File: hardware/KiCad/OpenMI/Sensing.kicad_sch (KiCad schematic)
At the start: 42 parts, among them U2 INA381A2IDGS, U5 MCP6004-SL, U7 MCP6001T-OT

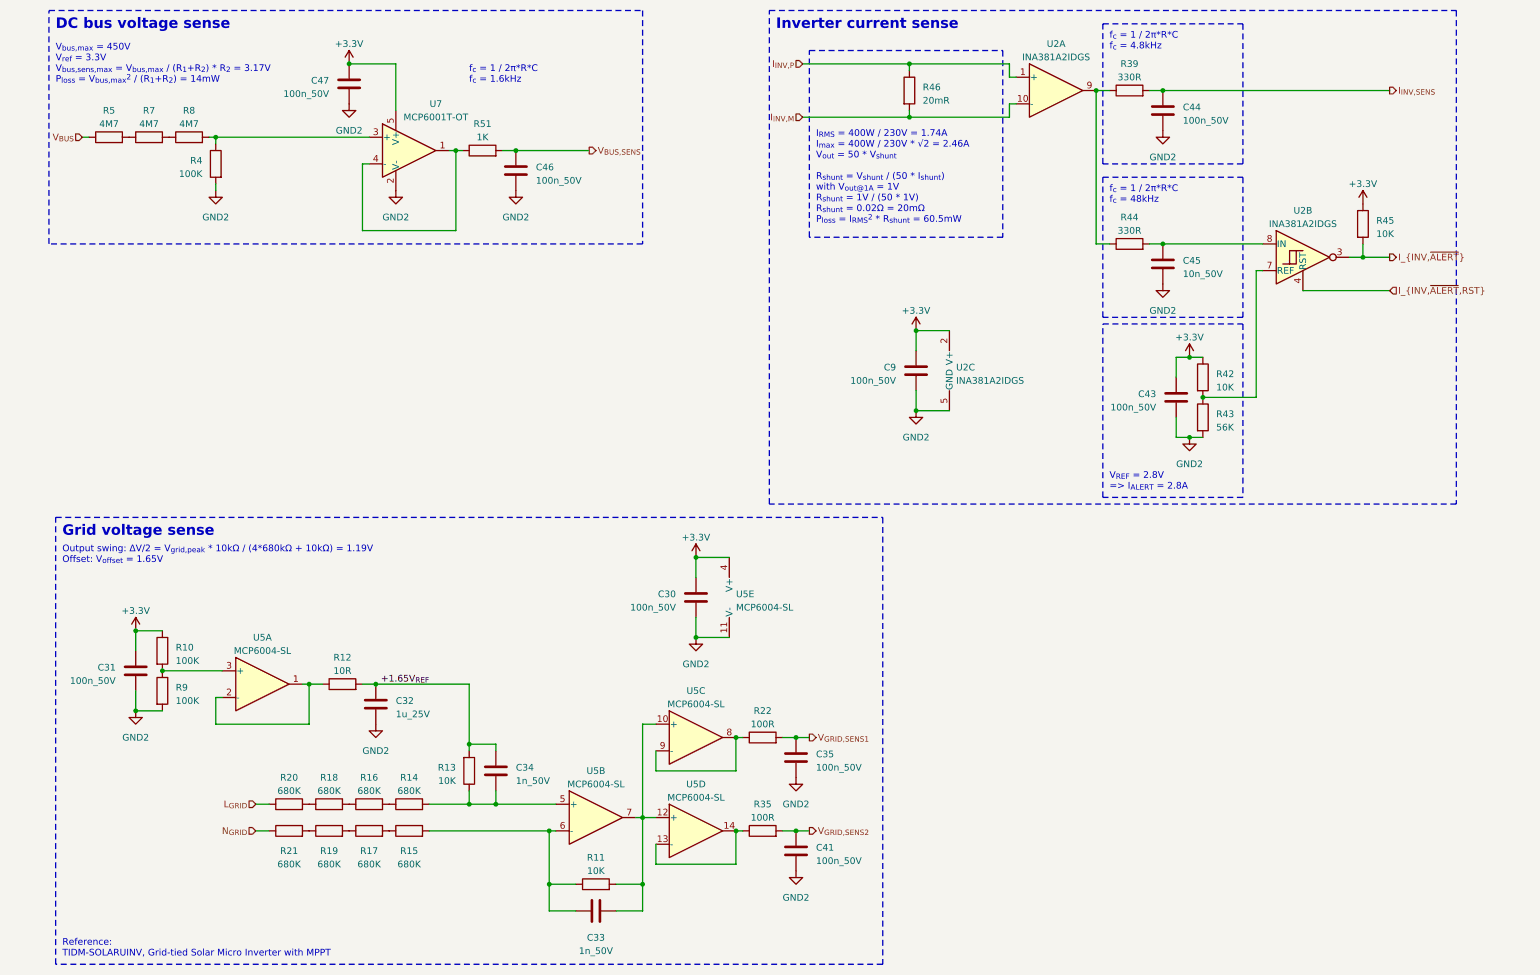
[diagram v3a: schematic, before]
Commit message: feat: Adds grid current sensing using a hall effect sensor.
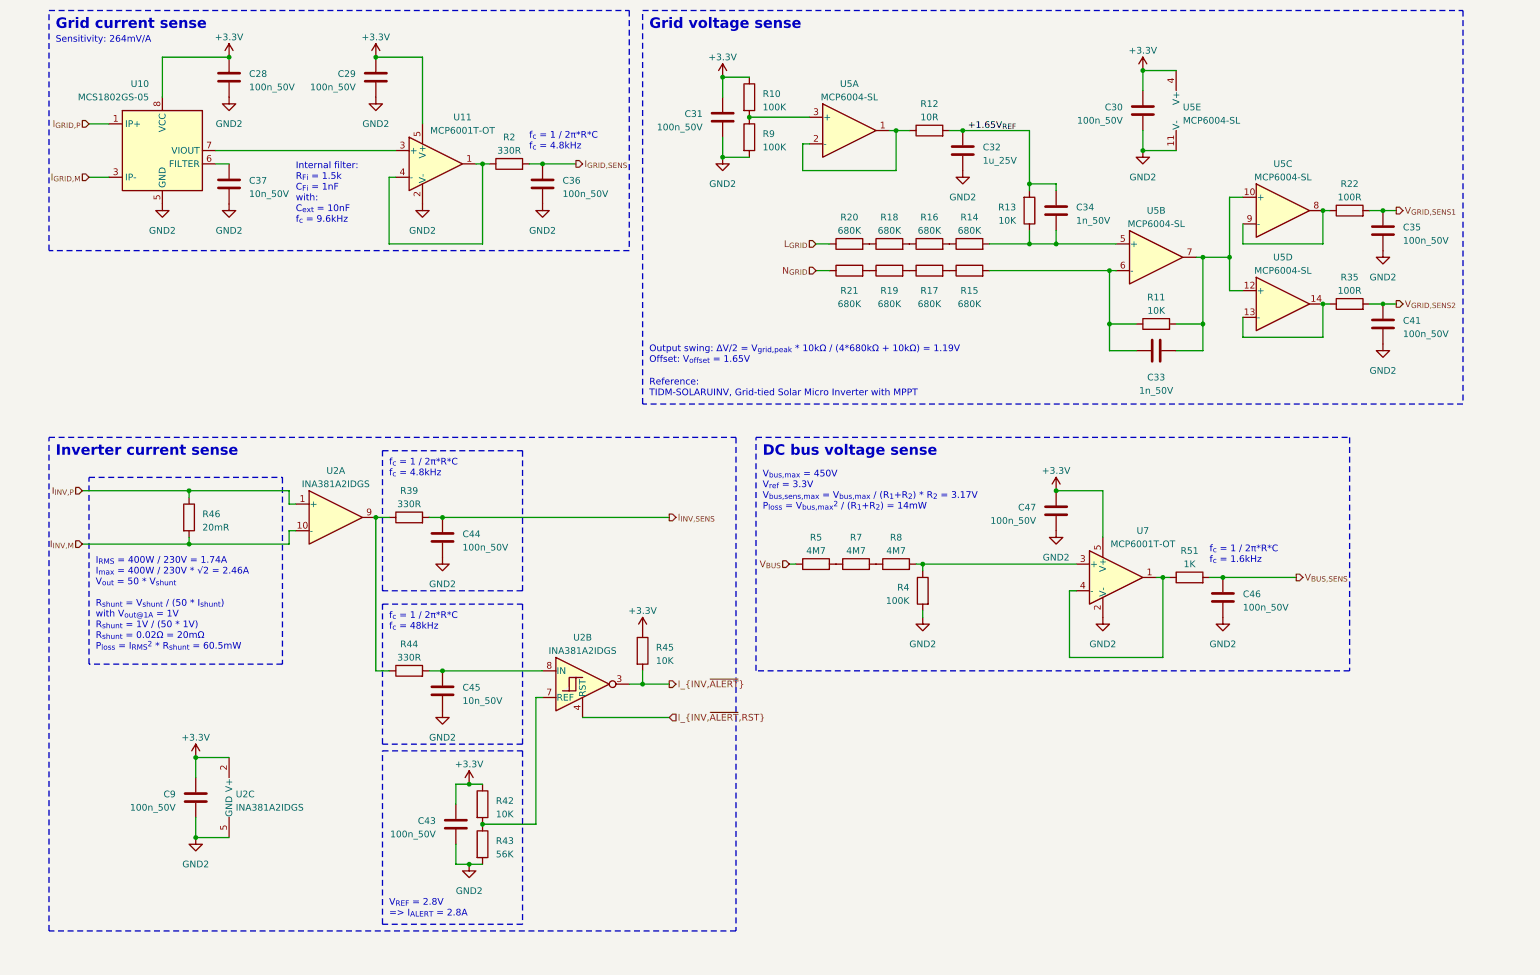
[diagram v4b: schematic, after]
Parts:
- added C28, C29, C36: 100n_50V, Capacitor_SMD:C_0603_1608Metric, symbol _C_0603:100n_50V
- added C37: 10n_50V, Capacitor_SMD:C_0603_1608Metric, symbol _C_0603:10n_50V
- added R2: 330R, Resistor_SMD:R_0603_1608Metric, symbol _R_0603:330R
- added U10: MCS1802GS-05, Package_SO:SOIC-8_3.9x4.9mm_P1.27mm, symbol _Amplifier_Current:MCS1802GS-05
- added U11: MCP6001T-OT, Package_TO_SOT_SMD:SOT-23-5, symbol _Amplifier_Operational:MCP6001T-OT
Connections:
- net +3.3V: now also C28.1, C29.1, U10.8 (VCC), U11.5 (V+)
- net GND2: now also C28.2, C29.2, C36.2, C37.2, U10.5 (GND), U11.2 (V-)
- new net: R2.1, U11.1, U11.4 (-)
- new net: U10.7 (VIOUT), U11.3 (+)
- new net: C37.1, U10.6 (FILTER)
- new net I_{GRID,M}: U10.3 (IP-), U10.4 (IP-)
- new net I_{GRID,P}: U10.1 (IP+), U10.2 (IP+)
- new net I_{GRID,SENS}: C36.1, R2.2
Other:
- note added: "Grid current sense"
- note added: "Internal filter: R_{Fi} = 1.5k C_{Fi} = 1nF with: C_{ext} = 10nF f_{c} = 9.6kHz"
- note added: "Sensitivity: 264mV/A"
- moved on the sheet: C30, C31, C32, C33, C34, C35, C41, C43, C44, C45, C46, C47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

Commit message: feat(hw): Adds grid current alert output to `Sensing`.
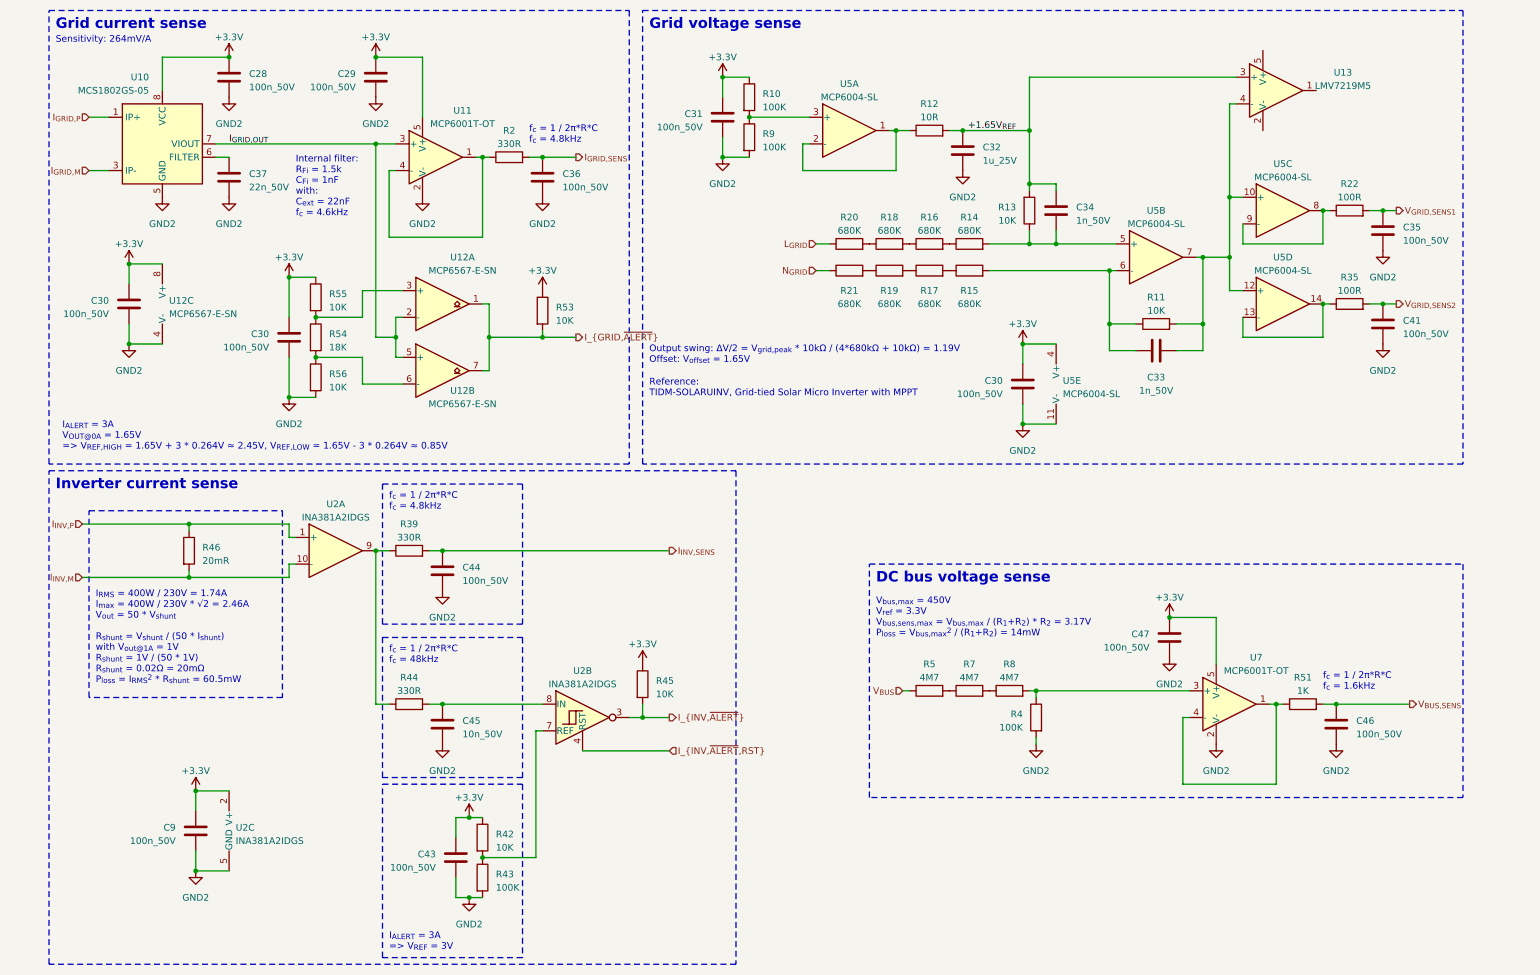
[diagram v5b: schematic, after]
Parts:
- removed C37: 10n_50V, Capacitor_SMD:C_0603_1608Metric, symbol _C_0603:10n_50V
- removed R43: 56K, Resistor_SMD:R_0603_1608Metric, symbol _R_0603:56K
- added C30 (x2): 100n_50V, Capacitor_SMD:C_0603_1608Metric, symbol _C_0603:100n_50V
- added C37: 22n_50V, Capacitor_SMD:C_0603_1608Metric, symbol _C_0603:22n_50V
- added R43: 100K, Resistor_SMD:R_0603_1608Metric, symbol _R_0603:100K
- added R53, R55, R56: 10K, Resistor_SMD:R_0603_1608Metric, symbol _R_0603:10K
- added R54: 18K, Resistor_SMD:R_0603_1608Metric, symbol _R_0603:18K
- added U12: MCP6567-E-SN, Package_SO:SOIC-8_3.9x4.9mm_P1.27mm, symbol _Comparator:MCP6567-E-SN
- added U13: LMV7219M5, Package_TO_SOT_SMD:SOT-23-5, symbol Comparator:LMV7219M5
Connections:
- net +1.65V_{REF}: now also U13.3 (+)
- net +3.3V: now also C30.1, C30.1, R53.1, R55.1, U12.8 (V+)
- net GND2: now also C30.2, C30.2, C37.2, R43.2, R56.2, U12.4 (V-)
- net at R42.2, U2.7 (REF): now also R43.1
- net I_{GRID,OUT}: now reaches U10.7 (VIOUT), U11.3 (+)
- net I_{GRID,OUT}: now also U12.2 (-), U12.5 (+)
- net at C33.2, R11.2, U5.10 (+)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: now also U13.4 (-)
- net at U10.6 (FILTER): now also C37.1
- new net: R54.1, R55.2, U12.3 (+)
- new net: R54.2, R56.1, U12.6 (-)
- new net I_{GRID,~{ALERT}}: R53.2, U12.1, U12.7
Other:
- note added: "I_{ALERT} = 3A => V_{REF} = 3V"
- note added: "I_{ALERT} = 3A V_{OUT@0A} = 1.65V => V_{REF,HIGH} = 1.65V + 3 * 0.264V ≈ 2.45V, V_{REF,LOW} = 1.65V - 3 * 0.264V ≈ 0.85V"
- note added: "Internal filter: R_{Fi} = 1.5k C_{Fi} = 1nF with: C_{ext} = 22nF f_{c} = 4.6kHz"
- note removed: "Internal filter: R_{Fi} = 1.5k C_{Fi} = 1nF with: C_{ext} = 10nF f_{c} = 9.6kHz"
- note removed: "V_{REF} = 2.8V => I_{ALERT} = 2.8A"
- moved on the sheet: C30, C36, C43, C44, C45, C46, C47, C9, R2, R39, R4, R42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

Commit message: feat(hw): Adds zero-crossing-detection (ZCD) to `Sensing`.
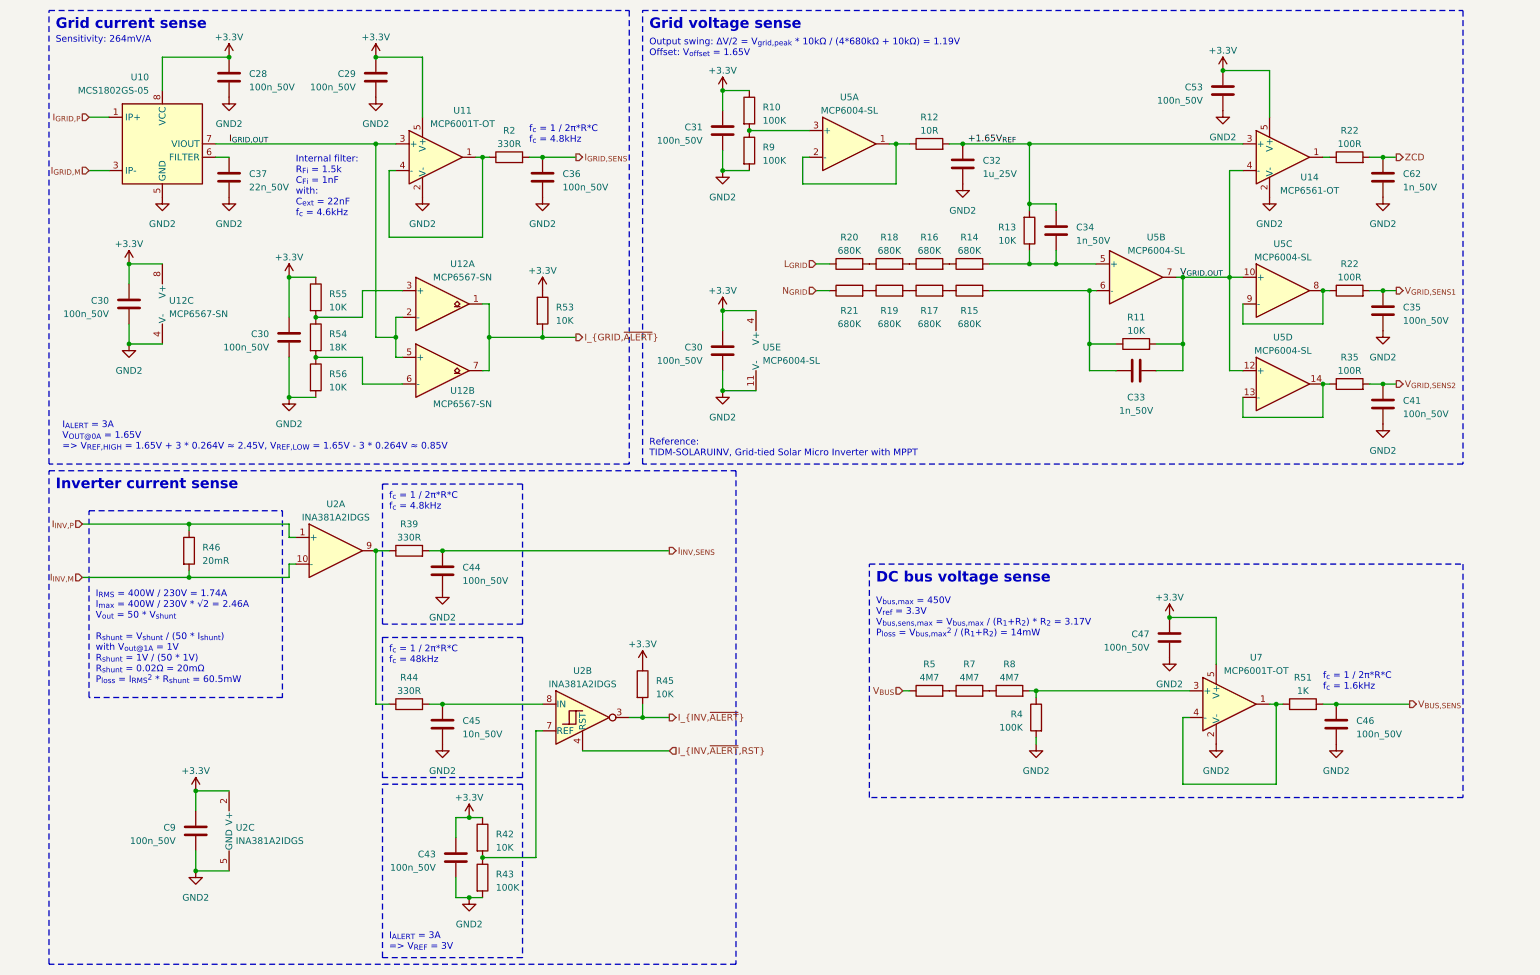
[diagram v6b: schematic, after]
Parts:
- removed U12: MCP6567-E-SN, Package_SO:SOIC-8_3.9x4.9mm_P1.27mm, symbol _Comparator:MCP6567-E-SN
- removed U13: LMV7219M5, Package_TO_SOT_SMD:SOT-23-5, symbol Comparator:LMV7219M5
- added C53: 100n_50V, Capacitor_SMD:C_0603_1608Metric, symbol _C_0603:100n_50V
- added C62: 1n_50V, Capacitor_SMD:C_0603_1608Metric, symbol _C_0603:1n_50V
- added R22: 100R, Resistor_SMD:R_0603_1608Metric, symbol _R_0603:100R
- added U12: MCP6567-SN, Package_SO:SOIC-8_3.9x4.9mm_P1.27mm, symbol _Comparator:MCP6567-SN
- added U14: MCP6561-OT, Package_TO_SOT_SMD:SOT-23-5, symbol _Comparator:MCP6561-OT
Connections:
- net +1.65V_{REF}: now also U14.3 (+)
- net +3.3V: now also C53.1, U12.8 (V+), U14.5 (V+)
- net GND2: now also C53.2, C62.2, U12.4 (V-), U14.2 (V-)
- net I_{GRID,OUT}: now also U12.2 (-), U12.5 (+)
- net I_{GRID,~{ALERT}}: now also U12.1, U12.7
- net at R54.1, R55.2: now also U12.3 (+)
- net V_{GRID,OUT}: now reaches C33.2, R11.2, U5.10 (+), U5.12 (+), U5.7
- net V_{GRID,OUT}: now also U14.4 (-)
- net at R54.2, R56.1: now also U12.6 (-)
- new net: R22.1, U14.1
- new net ZCD: C62.1, R22.2
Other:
- moved on the sheet: C30, C31, C32, C33, C34, C35, C41, R10, R11, R12, R13, R14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

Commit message: build(hw): Update library reference
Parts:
- removed U10: MCS1802GS-05, Package_SO:SOIC-8_3.9x4.9mm_P1.27mm, symbol _Amplifier_Current:MCS1802GS-05
- added U10: MCS1802GS-05, Package_SO:SOIC-8_3.9x4.9mm_P1.27mm, symbol _Sensor_Current:MCS1802GS-05
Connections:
- net +3.3V: now also U10.8 (VCC)
- net GND2: now also U10.5 (GND)
- net I_{GRID,M}: now also U10.3 (IP-), U10.4 (IP-)
- net I_{GRID,OUT}: now also U10.7 (VIOUT)
- net I_{GRID,P}: now also U10.1 (IP+), U10.2 (IP+)
- net at C37.1: now also U10.6 (FILTER)
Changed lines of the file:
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@@
+    )
+  )
+  (symbol (lib_id "_Sensor_Current:MCS1802GS-05") (at 35.56 39.37 0) (unit 1)
+    (in_bom yes) (on_board yes) (dnp no)
+    (property "Reference" "U10" (at 33.02 26.67 0)
+      (effects (font (size 1.27 1.27)) (justify right))
+    )
+    (property "Value" "MCS1802GS-05" (at 33.02 29.21 0)
+      (effects (font (size 1.27 1.27)) (justify right))
+    )
+    (property "Footprint" "Package_SO:SOIC-8_3.9x4.9mm_P1.27mm" (at 38.1 48.26 0)
+      (effects (font (size 1.27 1.27) italic) (justify left) hide)
+    )
+    (property "Datasheet" "https://www.monolithicpower.com/en/documentview/productdocument/index/version/2/document_type/Datasheet/lang/en/sku/MCS1802/" (at 35.56 39.37 0)
+      (effects (font (size 1.27 1.27)) hide)
+    )
+    (property "MF" "MPS" (at 35.56 39.37 0)
+      (effects (font (size 1.27 1.27)) hide)
+    )
+    (property "MPN" "MCS1802GS-05" (at 35.56 39.37 0)
+      (effects (font (size 1.27 1.27)) hide)
+    )
+    (property "OC_CONRAD" "" (at 35.56 39.37 0)
+      (effects (font (size 1.27 1.27)) hide)
+    )
+    (property "OC_FARNELL" "" (at 35.56 39.37 0)
+      (effects (font (size 1.27 1.27)) hide)
+    )
+    (property "OC_LCSC" "" (at 35.56 39.37 0)
+      (effects (font (size 1.27 1.27)) hide)
+    )
+    (property "OC_MOUSER" "946-MCS1802GS-05-P" (at 35.56 39.37 0)
+      (effects (font (size 1.27 1.27)) hide)
+    )
+    (property "OC_REICHELT" "" (at 35.56 39.37 0)
+      (effects (font (size 1.27 1.27)) hide)
+    )
+    (pin "1")
+    (pin "2")
+    (pin "3")
+    (pin "4")
+    (pin "5")
+    (pin "6")
+    (pin "7")
+    (pin "8")
+    (instances
+      (project "OpenMI"
+        (path "/2d959e19-1572-42a0-a8fd-da8463ad4e66/bb3056b4-4e5d-4f2d-baa2-a568d9d3e754"
+          (reference "U10") (unit 1)
+        )
+      )
     )
   )
@@
         )
       )
-    )
-  )
-  (symbol (lib_id "_Amplifier_Current:MCS1802GS-05") (at 35.56 39.37 0) (unit 1)
-    (in_bom yes) (on_board yes) (dnp no)
-    (property "Reference" "U10" (at 33.02 26.67 0)
-      (effects (font (size 1.27 1.27)) (justify right))
-    )
-    (property "Value" "MCS1802GS-05" (at 33.02 29.21 0)
-      (effects (font (size 1.27 1.27)) (justify right))
-    )
-    (property "Footprint" "Package_SO:SOIC-8_3.9x4.9mm_P1.27mm" (at 38.1 48.26 0)
-      (effects (font (size 1.27 1.27) italic) (justify left) hide)
-    )
-    (property "Datasheet" "https://www.monolithicpower.com/en/documentview/productdocument/index/version/2/document_type/Datasheet/lang/en/sku/MCS1802/" (at 35.56 39.37 0)
-      (effects (font (size 1.27 1.27)) hide)
-    )
-    (property "MF" "MPS" (at 35.56 39.37 0)
-      (effects (font (size 1.27 1.27)) hide)
-    )
-    (property "MPN" "MCS1802GS-05" (at 35.56 39.37 0)
-      (effects (font (size 1.27 1.27)) hide)
-    )
-    (property "OC_CONRAD" "" (at 35.56 39.37 0)
-      (effects (font (size 1.27 1.27)) hide)
-    )
-    (property "OC_FARNELL" "" (at 35.56 39.37 0)
-      (effects (font (size 1.27 1.27)) hide)
-    )
-    (property "OC_LCSC" "" (at 35.56 39.37 0)
-      (effects (font (size 1.27 1.27)) hide)
-    )
-    (property "OC_MOUSER" "946-MCS1802GS-05-P" (at 35.56 39.37 0)
-      (effects (font (size 1.27 1.27)) hide)
-    )
-    (property "OC_REICHELT" "" (at 35.56 39.37 0)
-      (effects (font (size 1.27 1.27)) hide)
-    )
-    (pin "1")
-    (pin "2")
-    (pin "3")
-    (pin "4")
-    (pin "5")
-    (pin "6")
-    (pin "7")
-    (pin "8")
-    (instances
-      (project "OpenMI"
-        (path "/2d959e19-1572-42a0-a8fd-da8463ad4e66/bb3056b4-4e5d-4f2d-baa2-a568d9d3e754"
-          (reference "U10") (unit 1)
-        )
-      )
